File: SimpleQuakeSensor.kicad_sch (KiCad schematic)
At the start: 38 parts, among them J1 Conn_Coaxial_Small, J2 Conn_Coaxial_Small, J3 Bat -12V GND, J4 Bat +12V, Q1 2N4401, Q2 BF245B, Q3 2N4401

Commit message: Add blocking capacitor
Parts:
- added C14: 10 uF, Capacitor_Tantalum_SMD:CP_EIA-2012-12_Kemet-R, symbol Device:C_Polarized
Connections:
- net at C11.1, Q3.3 (C), R8.1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: now also C14.1; no longer J2.1 (In)
- new net: C14.2, J2.1 (In)
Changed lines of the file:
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@@
+	(wire
+		(pts
+			(xy 199.39 60.96) (xy 199.39 68.58)
+		)
+		(stroke
+			(width 0)
+			(type default)
+		)
+	)
 	(wire
 		(pts
@@
 	(wire
 		(pts
-			(xy 199.39 68.58) (xy 199.39 50.8)
-		)
-		(stroke
-			(width 0)
-			(type default)
-		)
-	)
-	(wire
-		(pts
 			(xy 191.77 129.54) (xy 199.39 129.54)
 		)
@@
 		(pts
 			(xy 120.65 88.9) (xy 120.65 90.17)
+		)
+		(stroke
+			(width 0)
+			(type default)
+		)
+	)
+	(wire
+		(pts
+			(xy 199.39 50.8) (xy 199.39 53.34)
 		)
 		(stroke
@@
 					(unit 1)
 				)
+			)
+		)
+	)
+	(symbol
+		(lib_id "Device:C_Polarized")
+		(at 199.39 57.15 0)
+		(unit 1)
+		(body_style 1)
+		(exclude_from_sim no)
+		(in_bom yes)
+		(on_board yes)
+		(in_pos_files yes)
+		(dnp no)
+		(fields_autoplaced yes)
+		(property "Reference" "C14"
+			(at 203.2 54.9909 0)
+			(show_name no)
+			(do_not_autoplace no)
+			(effects
+				(font
+					(size 1.27 1.27)
+				)
+				(justify left)
+			)
+		)
+		(property "Value" "10 uF"
+			(at 203.2 57.5309 0)
+			(show_name no)
+			(do_not_autoplace no)
+			(effects
+				(font
+					(size 1.27 1.27)
+				)
+				(justify left)
+			)
+		)
+		(property "Footprint" "Capacitor_Tantalum_SMD:CP_EIA-2012-12_Kemet-R"
+			(at 200.3552 60.96 0)
+			(hide yes)
+			(show_name no)
+			(do_not_autoplace no)
+			(effects
+				(font
+					(size 1.27 1.27)
+				)
+			)
+		)
+		(property "Datasheet" ""
+			(at 199.39 57.15 0)
+			(hide yes)
+			(show_name no)
+			(do_not_autoplace no)
+			(effects
+				(font
+					(size 1.27 1.27)
+				)
+			)
+		)
+		(property "Description" "Polarized capacitor"
+			(at 199.39 57.15 0)
+			(hide yes)
+			(show_name no)
+			(do_not_autoplace no)
+			(effects
+				(font
+					(size 1.27 1.27)
+				)
+			)
+		)
+		(pin "2"
+		)
+		(pin "1"
+		)
+		(instances
+			(project "SimpleQuakeSensor"
+				(path "/3a27fe50-dd5f-4f6c-baa0-11a77565a9d6"
+					(reference "C14")
+					(unit 1)
+				)

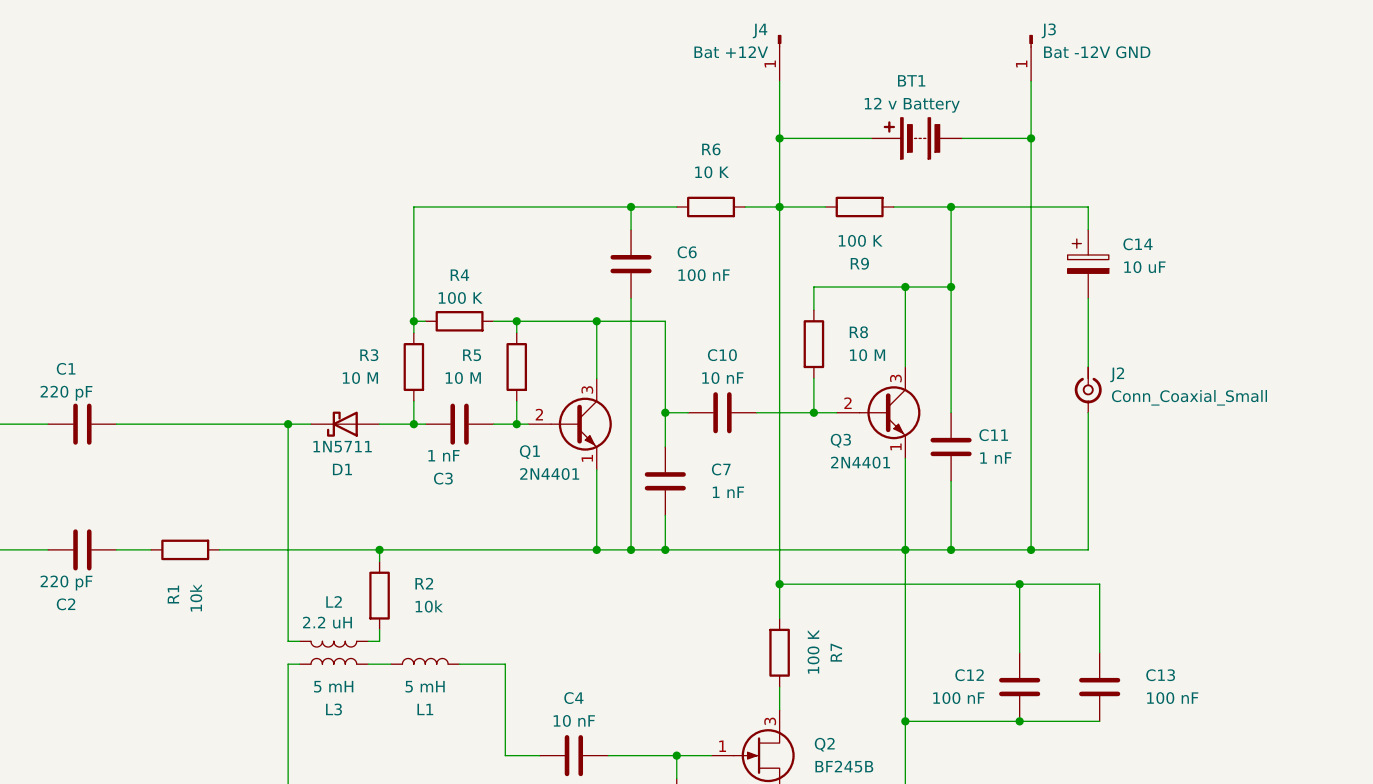
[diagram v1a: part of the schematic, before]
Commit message: Better impedance matching
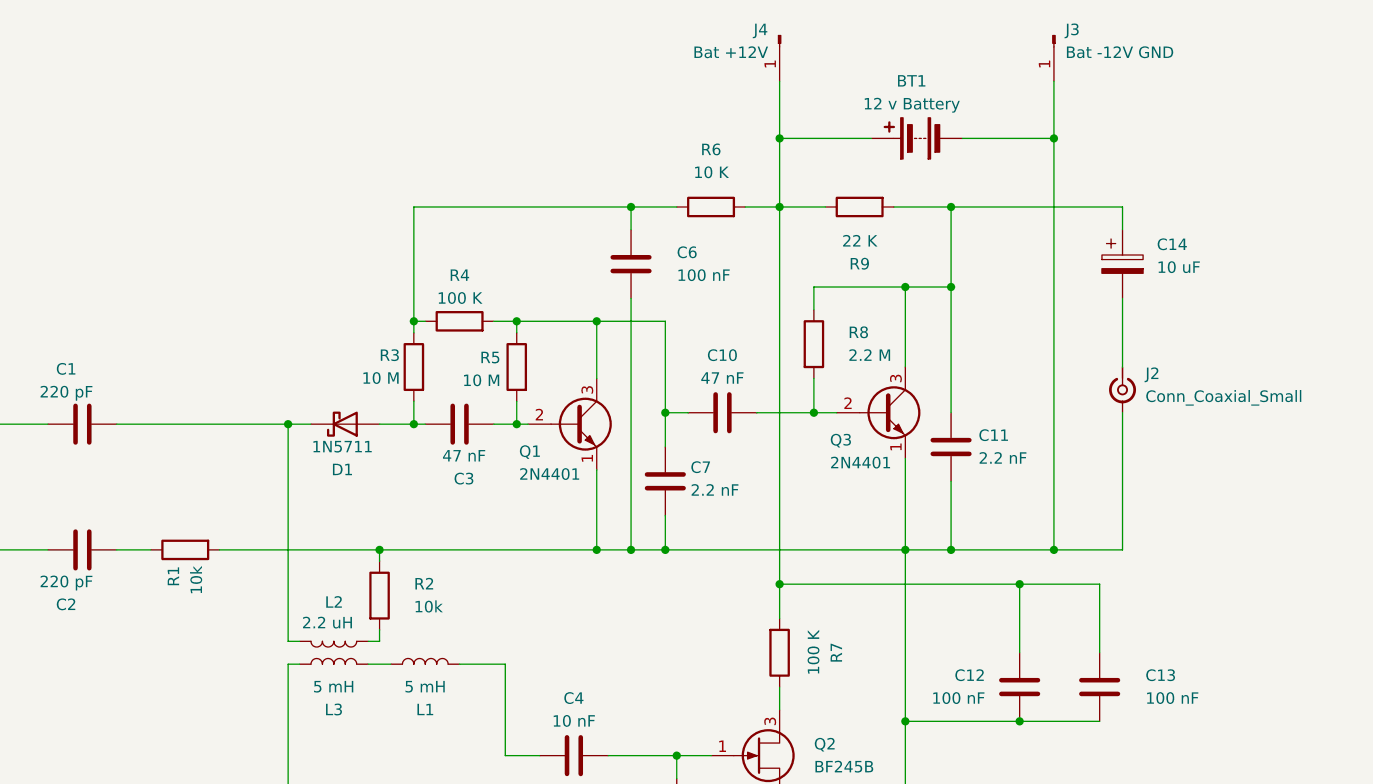
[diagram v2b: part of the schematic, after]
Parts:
- C10: value 10 nF -> 47 nF
- C11, C7: value 1 nF -> 2.2 nF
- C3: value 1 nF -> 47 nF
- R8: value 10 M -> 2.2 M
- R9: value 100 K -> 22 K
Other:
- moved on the sheet: C14, J2, J3
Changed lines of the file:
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@@
 	)
 	(junction
-		(at 184.15 50.8)
+		(at 165.1 43.18)
 		(diameter 0)
 		(color 0 0 0 0)
 	)
 	(junction
-		(at 165.1 43.18)
+		(at 179.07 59.69)
 		(diameter 0)
 		(color 0 0 0 0)
 	)
 	(junction
-		(at 179.07 59.69)
+		(at 191.77 137.16)
 		(diameter 0)
 		(color 0 0 0 0)
 	)
 	(junction
-		(at 191.77 137.16)
+		(at 195.58 88.9)
 		(diameter 0)
 		(color 0 0 0 0)
@@
 	)
 	(junction
-		(at 193.04 88.9)
-		(diameter 0)
-		(color 0 0 0 0)
-	)
-	(junction
 		(at 144.78 88.9)
 		(diameter 0)
@@
 	)
 	(junction
-		(at 179.07 88.9)
+		(at 184.15 50.8)
 		(diameter 0)
 		(color 0 0 0 0)
 	)
 	(junction
-		(at 110.49 74.93)
+		(at 179.07 88.9)
 		(diameter 0)
 		(color 0 0 0 0)
 	)
 	(junction
-		(at 193.04 43.18)
+		(at 110.49 74.93)
 		(diameter 0)
 		(color 0 0 0 0)
@@
 	)
 	(junction
+		(at 195.58 43.18)
+		(diameter 0)
+		(color 0 0 0 0)
+	)
+	(junction
 		(at 165.1 50.8)
 		(diameter 0)
@@
 	(wire
 		(pts
-			(xy 185.42 43.18) (xy 193.04 43.18)
+			(xy 185.42 43.18) (xy 195.58 43.18)
 		)
 		(stroke
@@
 	(wire
 		(pts
-			(xy 199.39 60.96) (xy 199.39 68.58)
+			(xy 203.2 60.96) (xy 203.2 68.58)
 		)
 		(stroke
@@
 	(wire
 		(pts
-			(xy 193.04 43.18) (xy 193.04 88.9)
+			(xy 195.58 43.18) (xy 195.58 88.9)
 		)
 		(stroke
@@
 	(wire
 		(pts
-			(xy 199.39 73.66) (xy 199.39 88.9)
+			(xy 203.2 73.66) (xy 203.2 88.9)
 		)
 		(stroke
@@
 	(wire
 		(pts
-			(xy 179.07 88.9) (xy 193.04 88.9)
+			(xy 179.07 88.9) (xy 195.58 88.9)
 		)
 		(stroke
@@
 	(wire
 		(pts
-			(xy 199.39 88.9) (xy 193.04 88.9)
+			(xy 203.2 88.9) (xy 195.58 88.9)
 		)
 		(stroke
@@
 	(wire
 		(pts
-			(xy 184.15 50.8) (xy 199.39 50.8)
+			(xy 184.15 50.8) (xy 203.2 50.8)
 		)
 		(stroke
@@
 	(wire
 		(pts
-			(xy 199.39 50.8) (xy 199.39 53.34)
+			(xy 203.2 50.8) (xy 203.2 53.34)
 		)
 		(stroke
@@
 	(wire
 		(pts
-			(xy 193.04 36.83) (xy 193.04 43.18)
+			(xy 195.58 36.83) (xy 195.58 43.18)
 		)
 		(stroke
@@
 			)
 		)
-		(property "Value" "1 nF"
+		(property "Value" "2.2 nF"
 			(at 187.198 78.74 0)
 			(show_name no)
@@
 			)
 		)
-		(property "Value" "10 nF"
+		(property "Value" "47 nF"
 			(at 158.75 69.85 90)
 			(show_name no)
@@
 			)
 		)
-		(property "Value" "10 M"
+		(property "Value" "2.2 M"
 			(at 172.72 67.3099 0)
 			(show_name no)
@@
 		(dnp no)
 		(property "Reference" "R3"
-			(at 120.65 67.3099 0)
+			(at 122.936 67.31 0)
 			(show_name no)
 			(do_not_autoplace no)
@@
 		)
 		(property "Value" "10 M"
-			(at 120.65 69.8499 0)
+			(at 122.936 69.85 0)
 			(show_name no)
 			(do_not_autoplace no)
@@
 		(dnp no)
 		(property "Reference" "R1"
-			(at 97.7899 92.71 0)
+			(at 97.79 90.678 0)
 			(show_name no)
 			(do_not_autoplace no)
@@
 		)
 		(property "Value" "10k"
-			(at 100.3299 92.71 0)
+			(at 100.33 90.678 0)
 			(show_name no)
 			(do_not_autoplace no)
@@
 	(symbol
 		(lib_id "Device:C_Polarized")
-		(at 199.39 57.15 0)
+		(at 203.2 57.15 0)
 		(unit 1)
 		(body_style 1)
@@
 		(fields_autoplaced yes)
 		(property "Reference" "C14"
-			(at 203.2 54.9909 0)
+			(at 207.01 54.9909 0)
 			(show_name no)
 			(do_not_autoplace no)
@@
 		)
 		(property "Value" "10 uF"
-			(at 203.2 57.5309 0)
+			(at 207.01 57.5309 0)
 			(show_name no)
 			(do_not_autoplace no)
@@
 		)
 		(property "Footprint" "Capacitor_Tantalum_SMD:CP_EIA-2012-12_Kemet-R"
-			(at 200.3552 60.96 0)
+			(at 204.1652 60.96 0)
 			(hide yes)
 			(show_name no)
@@
 		)
 		(property "Datasheet" ""
-			(at 199.39 57.15 0)
+			(at 203.2 57.15 0)
 			(hide yes)
 			(show_name no)
@@
 		)
 		(property "Description" "Polarized capacitor"
-			(at 199.39 57.15 0)
+			(at 203.2 57.15 0)
 			(hide yes)
 			(show_name no)
@@
 	(symbol
 		(lib_id "Connector:Conn_Coaxial_Small")
-		(at 199.39 71.12 270)
+		(at 203.2 71.12 270)
 		(unit 1)
 		(body_style 1)
@@
 		(fields_autoplaced yes)
 		(property "Reference" "J2"
-			(at 201.93 69.3303 90)
+			(at 205.74 69.3303 90)
 			(show_name no)
 			(do_not_autoplace no)
@@
 		)
 		(property "Value" "Conn_Coaxial_Small"
-			(at 201.93 71.8703 90)
+			(at 205.74 71.8703 90)
 			(show_name no)
 			(do_not_autoplace no)
@@
 		)
 		(property "Footprint" "Connector_Coaxial:SMA_Molex_73251-1153_EdgeMount_Horizontal"
-			(at 199.39 71.12 0)
+			(at 203.2 71.12 0)
 			(hide yes)
 			(show_name no)
@@
 		)
 		(property "Datasheet" ""
-			(at 199.39 71.12 0)
+			(at 203.2 71.12 0)
 			(hide yes)
 			(show_name no)
@@
 		)
 		(property "Description" "small coaxial connector (BNC, SMA, SMB, SMC, Cinch/RCA, LEMO, ...)"
-			(at 199.39 71.12 0)
+			(at 203.2 71.12 0)
 			(hide yes)
 			(show_name no)
@@
 		(in_pos_files yes)
 		(dnp no)
-		(fields_autoplaced yes)
 		(property "Reference" "C7"
-			(at 157.48 80.0099 0)
+			(at 155.194 79.756 0)
 			(show_name no)
 			(do_not_autoplace no)
@@
 			)
 		)
-		(property "Value" "1 nF"
-			(at 157.48 82.5499 0)
+		(property "Value" "2.2 nF"
+			(at 155.194 82.296 0)
 			(show_name no)
 			(do_not_autoplace no)
@@
 		(dnp no)
 		(property "Reference" "R5"
-			(at 132.08 67.3099 0)
+			(at 134.112 67.564 0)
 			(show_name no)
 			(do_not_autoplace no)
@@
 		)
 		(property "Value" "10 M"
-			(at 132.08 69.8499 0)
+			(at 134.112 70.104 0)
 			(show_name no)
 			(do_not_autoplace no)
@@
 	(symbol
 		(lib_id "Connector:Conn_01x01_Pin")
-		(at 193.04 31.75 270)
+		(at 195.58 31.75 270)
 		(unit 1)
 		(body_style 1)
@@
 		(fields_autoplaced yes)
 		(property "Reference" "J3"
-			(at 194.31 31.1149 90)
+			(at 196.85 31.1149 90)
 			(show_name no)
 			(do_not_autoplace no)
@@
 		)
 		(property "Value" "Bat -12V  GND"
-			(at 194.31 33.6549 90)
+			(at 196.85 33.6549 90)
 			(show_name no)
 			(do_not_autoplace no)
@@
 		)
 		(property "Footprint" "fmd-laser-libs:PinHeader_1x01_P2.54mm_Vertical_2_FMD"
-			(at 193.04 31.75 0)
+			(at 195.58 31.75 0)
 			(hide yes)
 			(show_name no)
@@
 		)
 		(property "Datasheet" ""
-			(at 193.04 31.75 0)
+			(at 195.58 31.75 0)
 			(hide yes)
 			(show_name no)
@@
 		)
 		(property "Description" "Generic connector, single row, 01x01, script generated"
-			(at 193.04 31.75 0)
+			(at 195.58 31.75 0)
 			(hide yes)
 			(show_name no)
@@
 			)
 		)
-		(property "Value" "100 K"
+		(property "Value" "22 K"
 			(at 173.99 54.61 90)
 			(show_name no)
@@
 		(dnp no)
 		(property "Reference" "C3"
-			(at 127.762 81.026 90)
+			(at 130.048 81.026 90)
 			(show_name no)
 			(do_not_autoplace no)
@@
 			)
 		)
-		(property "Value" "1 nF"
-			(at 127.762 78.486 90)
+		(property "Value" "47 nF"
+			(at 130.048 78.486 90)
 			(show_name no)
 			(do_not_autoplace no)

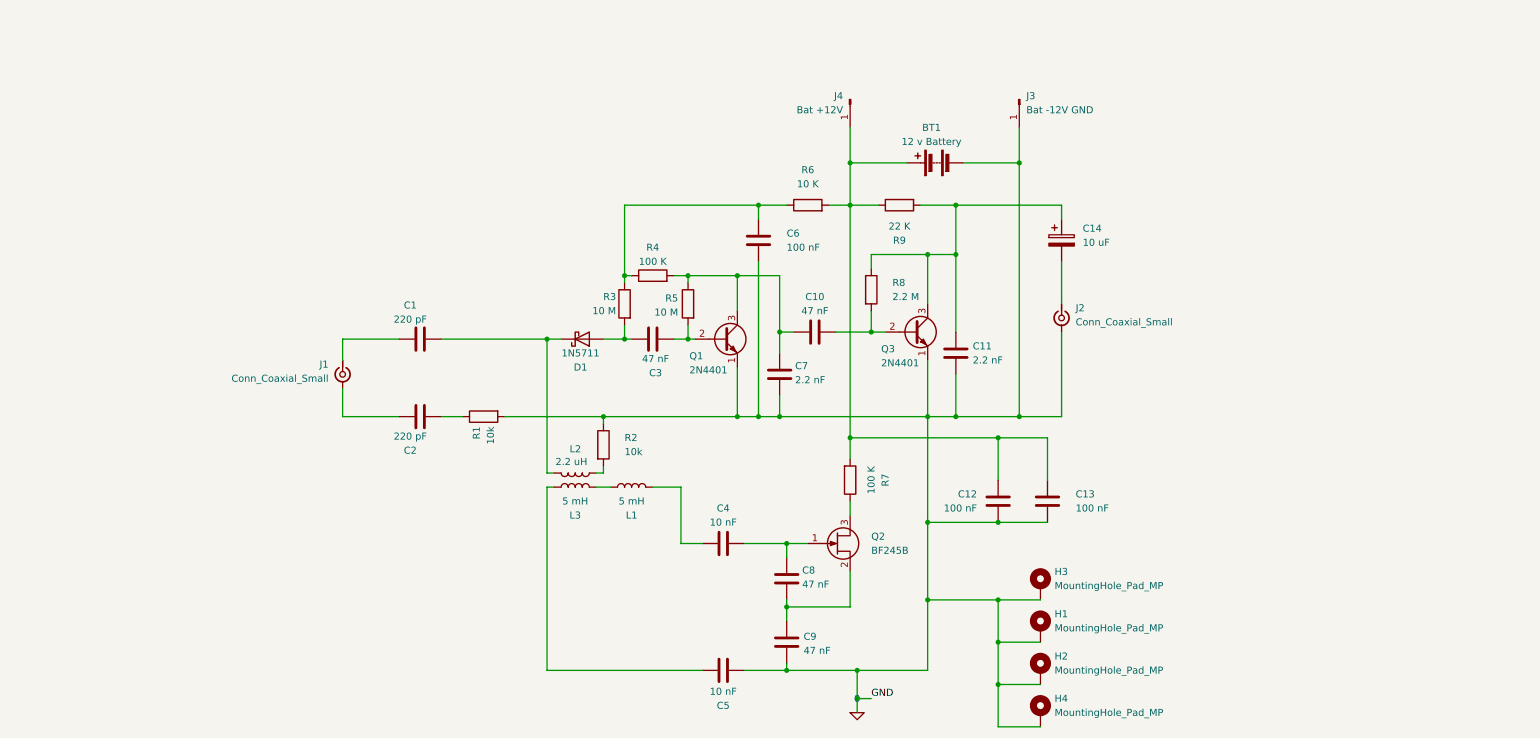
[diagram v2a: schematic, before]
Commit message: Updating osc, potentiometers, models, licence logo
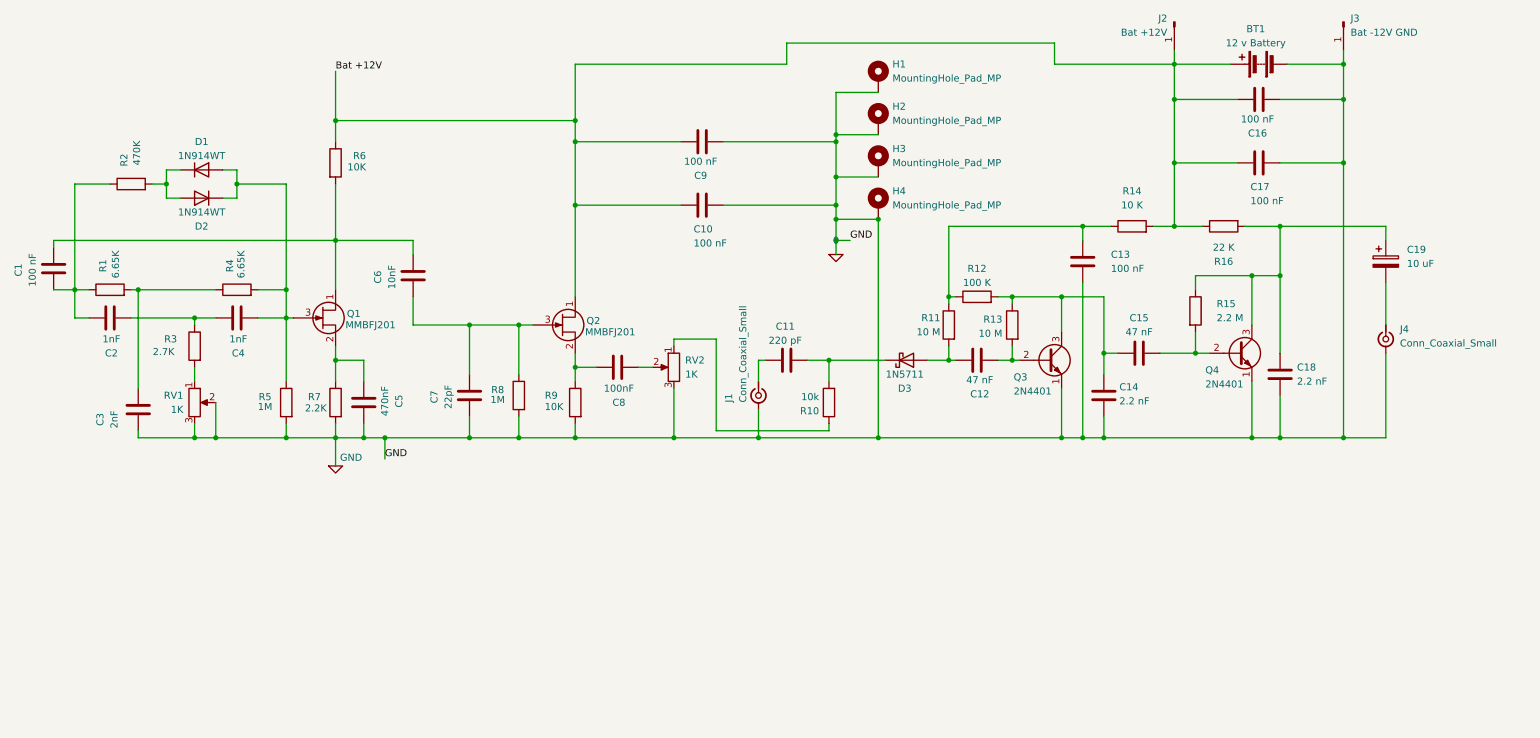
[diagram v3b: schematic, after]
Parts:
- removed L1, L3: 5 mH, Inductor_SMD:L_0805_2012Metric, symbol Device:L
- removed L2: 2.2 uH, Inductor_SMD:L_0805_2012Metric, symbol Device:L
- removed Q2: BF245B, Package_TO_SOT_SMD:SOT-23-3, symbol Transistor_FET:BF245B
- added C1, C10: 100 nF, Capacitor_SMD:C_0805_2012Metric, symbol Device:C
- added C3: 2nF, Capacitor_SMD:C_0805_2012Metric, symbol Device:C
- added C6: 10nF, Capacitor_SMD:C_0805_2012Metric, symbol Device:C
- added C7: 22pF, Capacitor_SMD:C_0805_2012Metric, symbol Device:C
- added D1, D2: 1N914WT, Diode_SMD:D_0805_2012Metric, symbol Diode:1N914WT
- added Q1, Q2: MMBFJ201, Package_TO_SOT_SMD:SOT-23-3, symbol Device:Q_NJFET_DSG
- added R2: 470K, Resistor_SMD:R_0805_2012Metric, symbol Device:R
- added R3: 2.7K, Resistor_SMD:R_0805_2012Metric, symbol Device:R
- added R4: 6.65K, Resistor_SMD:R_0805_2012Metric, symbol Device:R
- added R5, R8: 1M, Resistor_SMD:R_0805_2012Metric, symbol Device:R
- added R6, R9: 10K, Resistor_SMD:R_0805_2012Metric, symbol Device:R
- added RV1, RV2: 1K, Potentiometer_SMD:Potentiometer_Bourns_TC33X_Vertical, symbol Device:R_Potentiometer
- C11: renamed from C1; footprint Capacitor_SMD:C_1206_3216Metric -> Capacitor_SMD:C_0805_2012Metric
- C19: renamed from C14; footprint Capacitor_Tantalum_SMD:CP_EIA-2012-12_Kemet-R -> Capacitor_Tantalum_SMD:CP_EIA-2012-15_AVX-P
- C2: value 220 pF -> 1nF; footprint Capacitor_SMD:C_1206_3216Metric -> Capacitor_SMD:C_0805_2012Metric
- C4: value 10 nF -> 1nF
- C5: value 10 nF -> 470nF
- C8: value 47 nF -> 100nF
- C9: value 47 nF -> 100 nF
- D3: renamed from D1; footprint Diode_SMD:D_1206_3216Metric -> Diode_SMD:D_0805_2012Metric
- R1: value 10k -> 6.65K
- R7: value 100 K -> 2.2K
- renumbered C3 to C12, C6 to C13, C7 to C14, C10 to C15, C13 to C16, C12 to C17, C11 to C18, H3 to H1, H1 to H2, H2 to H3, J4 to J2, J2 to J4, Q1 to Q3, Q3 to Q4, R2 to R10, R3 to R11, R4 to R12, R5 to R13, R6 to R14, R8 to R15, R9 to R16
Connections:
- net 0: now also C5.1, J1.2 (Ext), R7.2, C10.1, C3.1, C7.2, R5.2, R8.2, R9.2, RV1.2, RV1.3, RV2.3; no longer C5.2, R1.2, R10.1
- net Bat +12V: now reaches BT1.1 (+), C16.1, C17.2, J2.1 (Pin_1), R14.2, R16.1
- net Bat +12V: now also C9.1, C10.2, Q2.1 (D), R6.1; no longer R7.2
- net at C8.1: now also Q2.2 (S), R9.1; no longer C9.1
- net at R7.1: now also C5.2, Q1.2 (S)
- net at R10.2: now also C11.2, D3.1 (K)
- net at C2.2: now also C4.1, R3.1; no longer R1.1
- net at C8.2: now also RV2.2; no longer C4.2
- net at C2.1: now also R1.1, C1.2, R2.1; no longer J1.2 (Ext)
- new net: R3.2, RV1.1
- new net: C3.2, R1.2, R4.1
- new net: R10.1, RV2.1
- new net: C4.2, D1.2 (A), D2.1 (K), Q1.3 (G), R4.2, R5.1
- new net: D1.1 (K), D2.2 (A), R2.2
- new net: C1.1, C6.1, Q1.1 (D), R6.2
- new net: C6.2, C7.1, Q2.3 (G), R8.1
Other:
- moved on the sheet: BT1, C11, C12, C13, C14, C15, C16, C17, C18, C19, D3, H1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

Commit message: PCB update
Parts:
- R14: value 10 K -> 1 K
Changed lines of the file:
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@@
 			)
 		)
-		(property "Value" "10 K"
+		(property "Value" "1 K"
 			(at 215.9 50.8 90)
 			(show_name no)
